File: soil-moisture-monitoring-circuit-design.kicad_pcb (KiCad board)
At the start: 2 copper layers, 38.1 x 33 mm, 9 parts, among them J1 Conn_01x05_Analog_Soil_moistu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, J3 Conn_01x04_I2C_Soil_moisture, U1 DPT_Walter, U2 904, U3 904, U4 2465, U5 254, U6 BME680

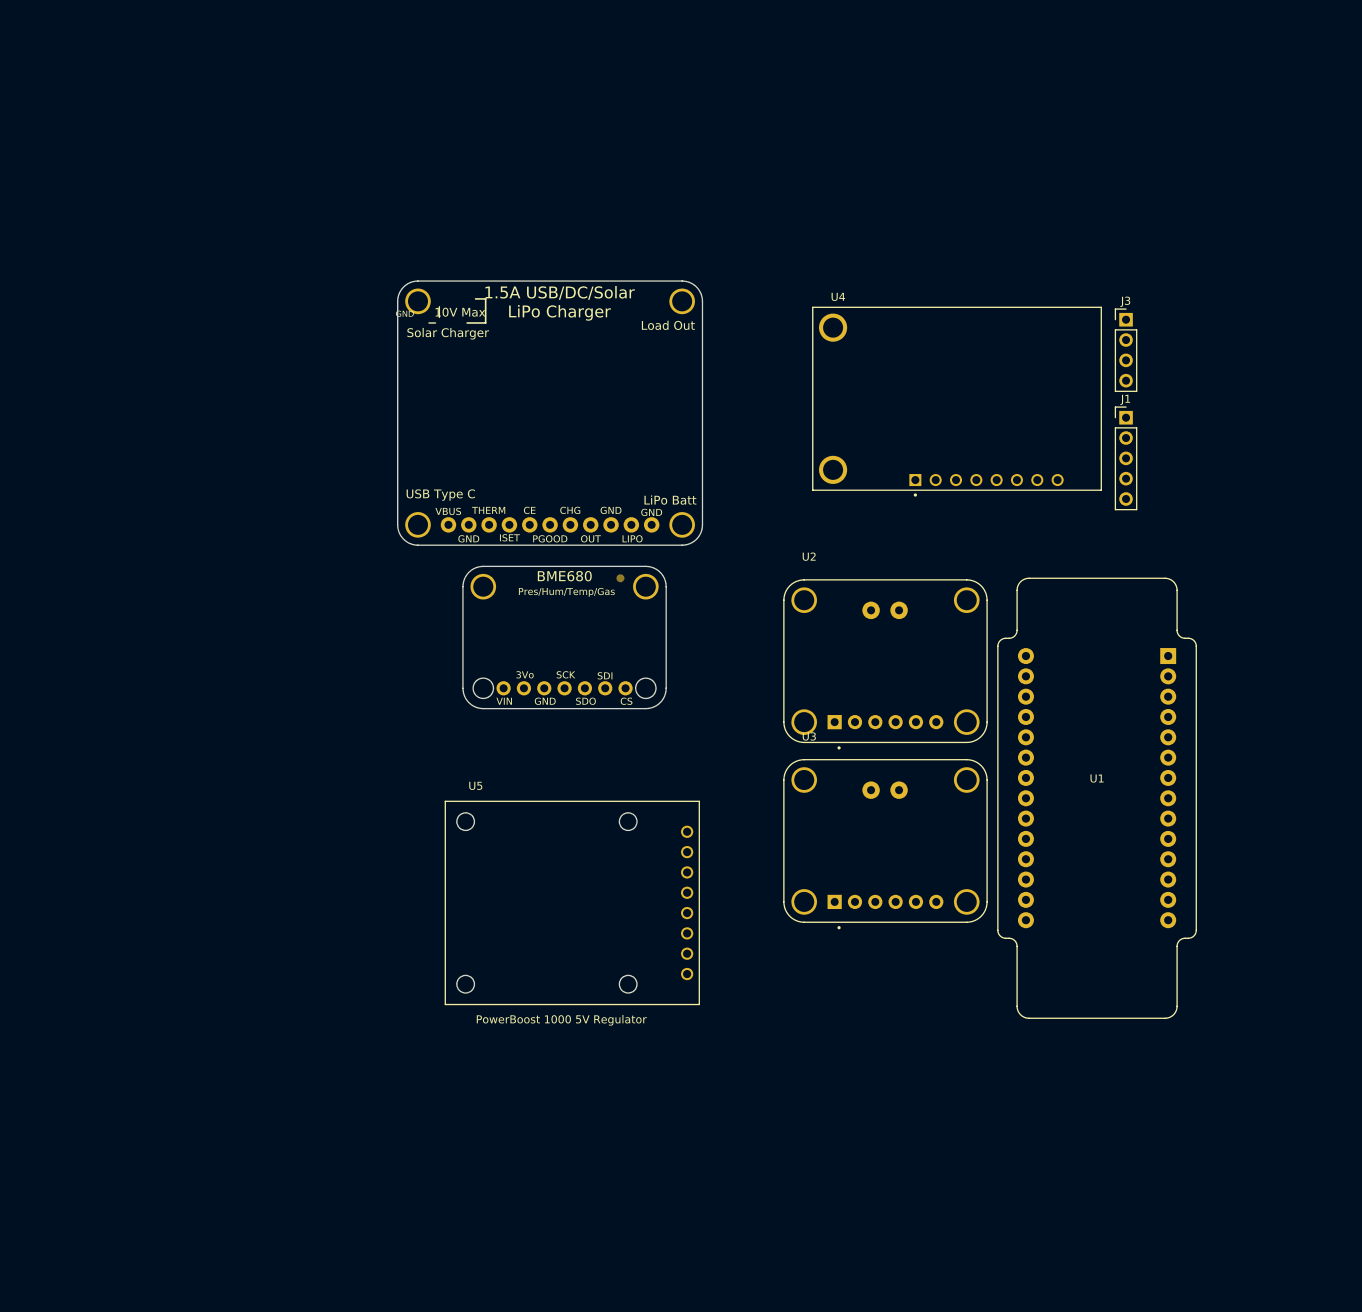
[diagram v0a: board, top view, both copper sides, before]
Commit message: Initial placement and routing
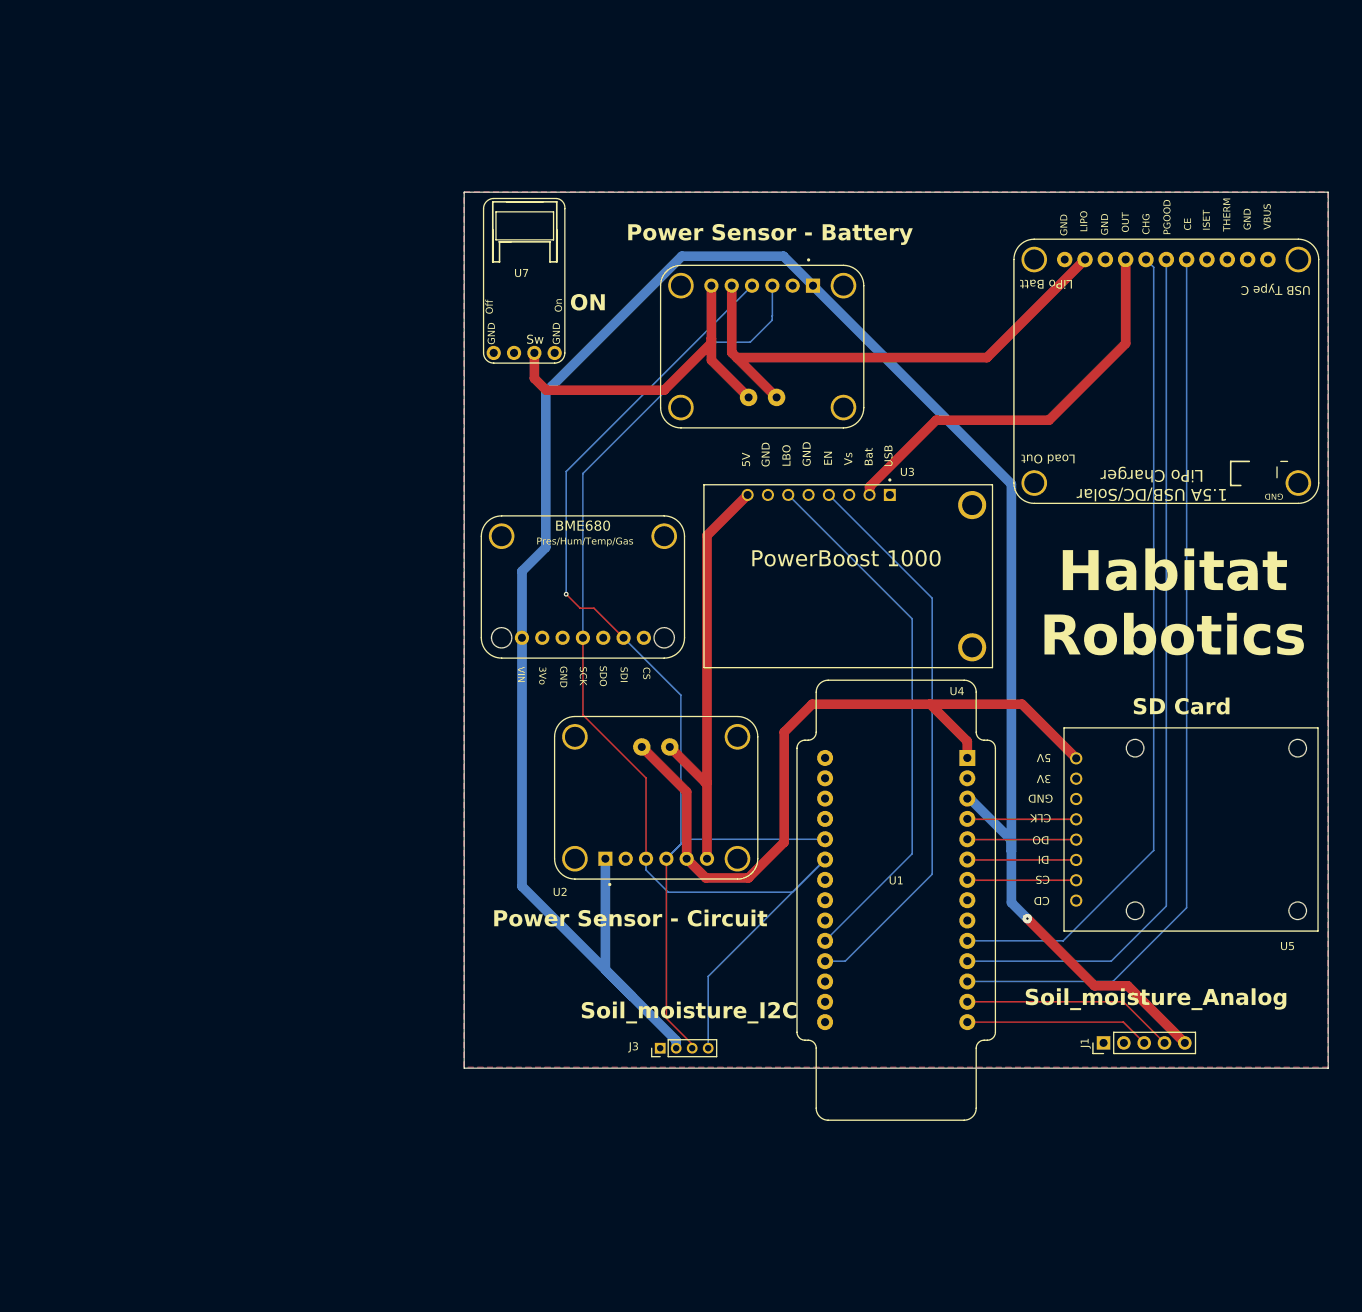
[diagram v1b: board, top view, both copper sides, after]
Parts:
- added U7: Switch1, Adafruit_Switch_JST:Adafruit_Switch_JST, F.Cu at (101.2, 50.6)
- J3: footprint Connector_PinHeader_2.54mm:PinHeader_1x04_P2.54mm_Vertical -> Connector_PinHeader_2.00mm:PinHeader_1x04_P2.00mm_Vertical
- moved J3 108.1 mm to (118.5, 147.0), turned to 90 degrees
- moved U3 82.7 mm to (143.9, 49.1), turned to 180 degrees
- moved J1 78.2 mm to (173.9, 146.3), turned to 90 degrees
- moved U5 77.9 mm to (184.9, 119.7), turned to 180 degrees
- moved Adafruit_BQ24074 77.7 mm to (182.0, 62.5), turned to 180 degrees
- moved U2 33.4 mm to (105.3, 125.9)
- moved U1 28.2 mm to (148.0, 127.2)
- moved U4 26.0 mm to (142.0, 88.0), turned to 180 degrees
- moved U6 6.72 mm to (108.8, 89.1)
- renumbered Adafruit_BQ1 to Adafruit_BQ24074
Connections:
- U1 pad 10: BOOST_EN -> LBO
- U1 pad 11: LBO -> BOOST_EN
- U1 pad 12: I2C_SDA -> unconnected-(U1-IO42-Pad12)
- U1 pad 13: I2C_SCL -> unconnected-(U1-IO2-Pad13)
- U1 pad 14: ANALOG_IN1 -> unconnected-(U1-IO1-Pad14)
- U1 pad 15: ANALOG_IN2 -> ANALOG_IN1
- U1 pad 16: unconnected-(U1-IO5-Pad16) -> ANALOG_IN2
- U1 pad 17: unconnected-(U1-IO6-Pad17) -> ~{CHARGE_EN}
- U1 pad 18: unconnected-(U1-IO7-Pad18) -> PGOOD
- U1 pad 19: unconnected-(U1-IO15-Pad19) -> CHG_STATUS
- U1 pad 2: ~{CAN_EN} -> unconnected-(U1-RX0/IO44-Pad2)
- U1 pad 23: CLK -> ESP32_DO
- U1 pad 25: ESP32_DO -> CLK
- U1 pad 3: 12V_EN -> unconnected-(U1-TX0/IO43-Pad3)
- U1 pad 7: ~{CHARGE_EN} -> unconnected-(U1-IO13-Pad7)
- U1 pad 8: PGOOD -> unconnected-(U1-IO38-Pad8)
- U1 pad 9: CHG_STATUS -> unconnected-(U1-IO39-Pad9)
- U2 pad 6: VCC+5+ -> VCC_5+
- U2 pad VIN+: VCC+5+ -> VCC_5+
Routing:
- net +3.3V: track 0.00 -> 277.1 mm, vias 0 -> 1
- net I2C_SCL: track 0.00 -> 143.6 mm
- net I2C_SDA: track 0.00 -> 134.8 mm, vias 0 -> 1
- net ~{CHARGE_EN}: track 0.00 -> 112.3 mm
- net PGOOD: track 0.00 -> 108.5 mm
- net CHG_STATUS: track 0.00 -> 102.2 mm
- net VCC_5-: track 0.00 -> 94.5 mm
- net BOOST_EN: track 0.00 -> 70.7 mm
- net LBO: track 0.00 -> 66.7 mm
- net LIPO-: track 0.00 -> 64.9 mm
- net VCC_5+: track 0.00 -> 54.1 mm
- net VCHARG: track 0.00 -> 50.9 mm
- net LIPO+: track 0.00 -> 44.9 mm
- net ANALOG_IN2: track 0.00 -> 26.8 mm
- net ANALOG_IN1: track 0.00 -> 23.2 mm
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- added copper zone on B.Cu, net GND
- added copper zone on F.Cu, net GND
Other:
- board size 38.1 x 33 mm -> 108 x 109.5 mm
- board text added: "Habitat Robotics"
- board text added: "ON"
- board text added: "Power Sensor - Battery"
- board text added: "Power Sensor - Circuit"
- board text added: "PowerBoost 1000"
- board text added: "SD Card"
- board text added: "Soil_moisture_Analog"
- board text added: "Soil_moisture_I2C"

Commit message: updated simplified design from Karun Potty
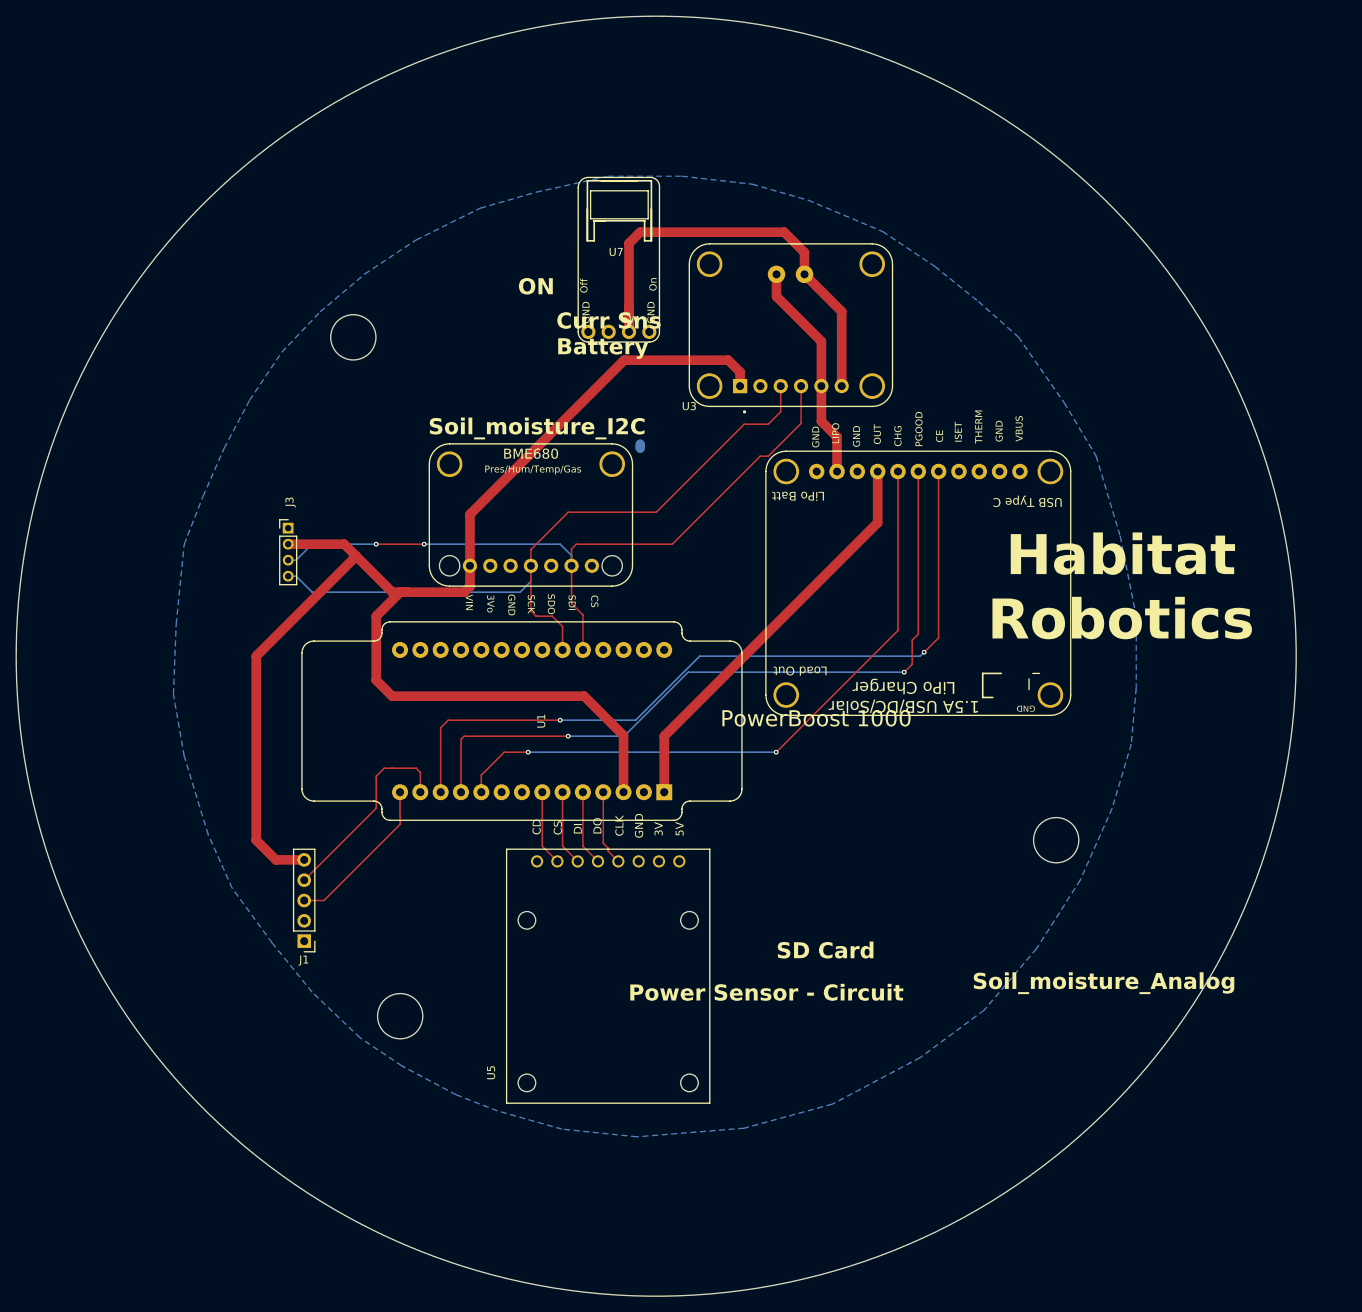
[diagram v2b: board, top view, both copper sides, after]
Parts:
- removed U2: 904, Adafruit_INA219:MODULE_904
- removed U4: 2465, Adafruit_Powerboost1000:MODULE_2465
- moved J1 100.7 mm to (74.0, 133.6), turned to 180 degrees
- moved J3 79.9 mm to (72.0, 82.0), turned to 0 degrees
- moved U5 75.1 mm to (112.0, 138.0), turned to 90 degrees
- moved U1 50.2 mm to (102.5, 106.1), turned to -90 degrees
- moved Adafruit_BQ24074 40.8 mm to (151.0, 89.0)
- moved U3 28.0 mm to (122.1, 66.8), turned to 0 degrees
- moved U7 12.1 mm to (113.0, 48.0)
- moved U6 11.1 mm to (102.3, 80.1)
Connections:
- U1 pad 28: VCC_5- -> VCHARG
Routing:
- net +3.3V: track 277.1 -> 180.4 mm, vias 1 -> 0
- net VCC_5-: track 94.5 -> 0.00 mm
- net BOOST_EN: track 70.7 -> 0.00 mm
- net LBO: track 66.7 -> 0.00 mm
- net VCC_5+: track 54.1 -> 0.00 mm
- net I2C_SCL: track 143.6 -> 90.6 mm
- net I2C_SDA: track 134.8 -> 91.2 mm, vias 1 -> 2
- net LIPO-: track 64.9 -> 27.8 mm
- net CHG_STATUS: track 102.2 -> 81.6 mm, vias 0 -> 2
- net PGOOD: track 108.5 -> 91.3 mm, vias 0 -> 2
- net ~{CHARGE_EN}: track 112.3 -> 95.7 mm, vias 0 -> 2
- net LIPO+: track 44.9 -> 56.3 mm
- net ESP32_DO: track 13.6 -> 9.43 mm
- net ESP32_DI: track 13.6 -> 9.43 mm
- net CS: track 13.6 -> 9.43 mm
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- removed copper zone on F.Cu, net GND
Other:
- board size 108 x 109.5 mm -> 160 x 160 mm
- board text added: "Curr Sns Battery"
- board text removed: "Power Sensor - Battery"

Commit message: outline of 122mm diameter
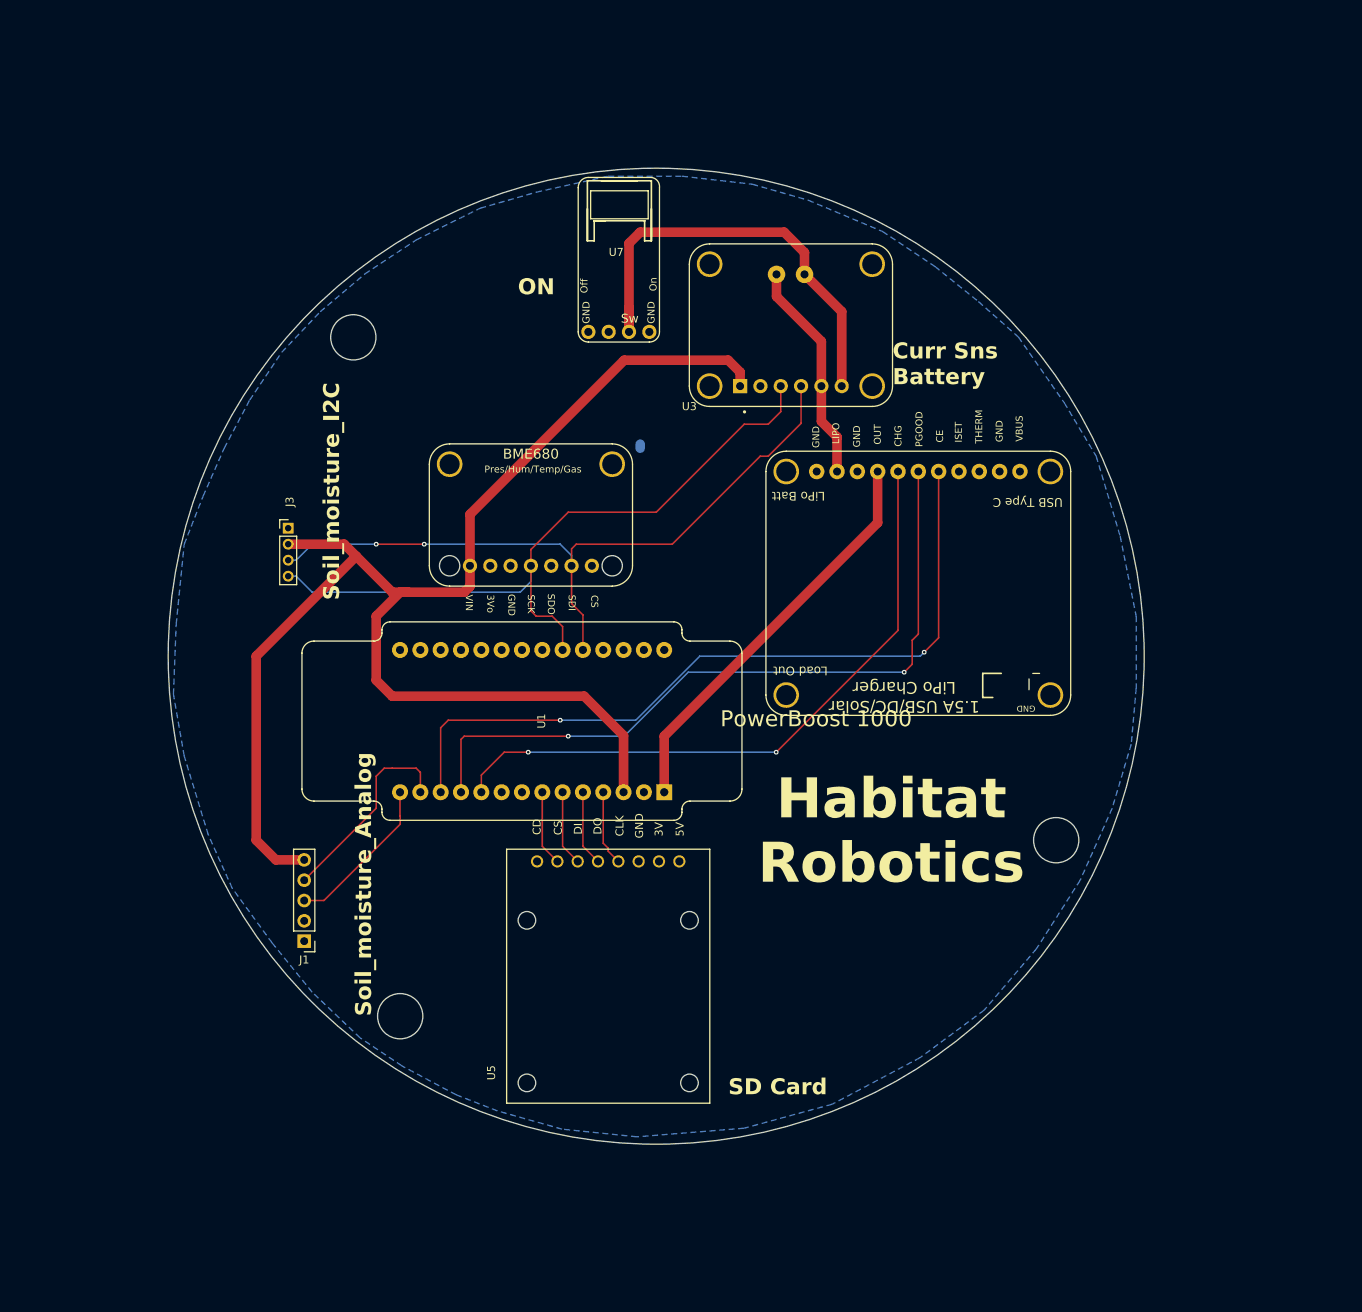
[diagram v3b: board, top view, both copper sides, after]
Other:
- board size 160 x 160 mm -> 122 x 122 mm
- board text removed: "Power Sensor - Circuit"
